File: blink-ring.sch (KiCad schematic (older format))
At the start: 35 parts, among them SW1 SW_SPDT, U1 ATtiny85_QFN20_1-5, U2 ATtiny85_QFN20_11-15

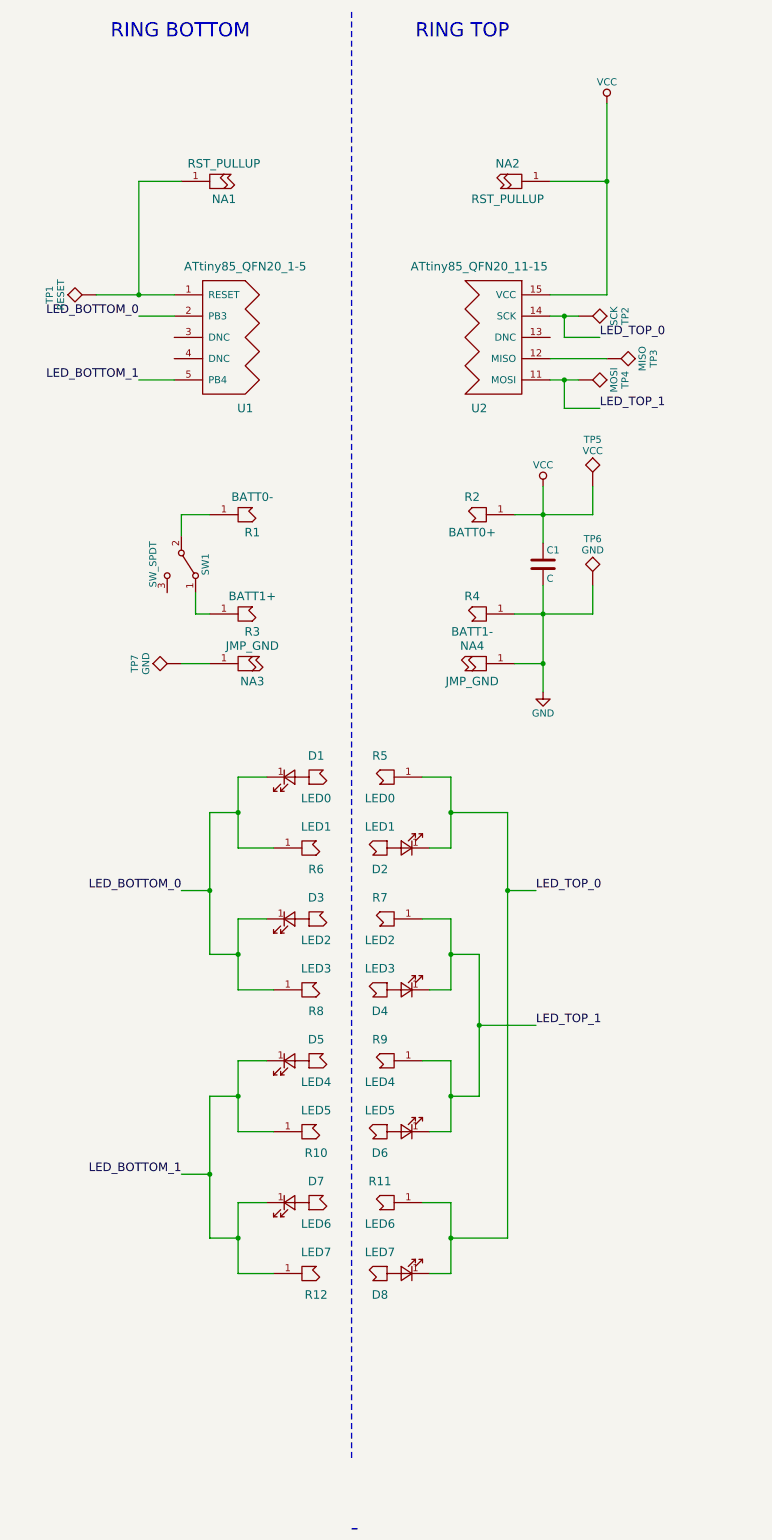
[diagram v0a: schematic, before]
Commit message: finalized PCB outline and layout. ordered first rev.
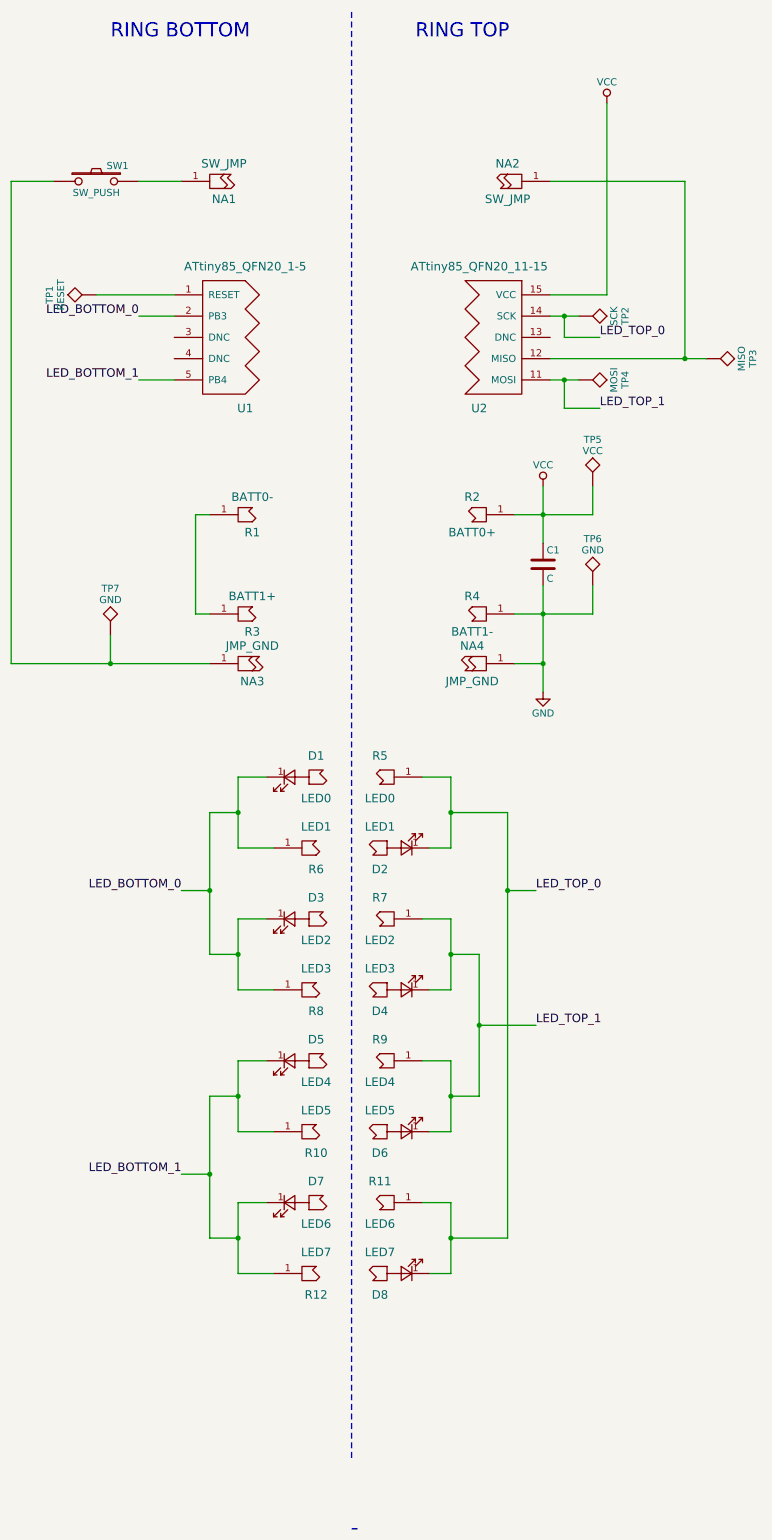
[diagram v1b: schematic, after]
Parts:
- removed SW1: SW_SPDT, KiCad_Footprints:ZF_SW_PCM12SMTR, symbol SW_SPDT
- added SW1: SW_PUSH, KiCad_Footprints:ZF_SW_B3U, symbol SW_PUSH
- NA1, NA2: value RST_PULLUP -> SW_JMP
- R1, R4: footprint KiCad_Footprints:ZF_STRUCT_2-2_HOLE -> KiCad_Footprints:ZF_BATT_AC10E_NEG
- R2, R3: footprint KiCad_Footprints:ZF_STRUCT_2-2_HOLE -> KiCad_Footprints:ZF_BATT_AC10E_POS
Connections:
- net VCC: no longer NA2.1
- net at TP1.1, U1.1 (RESET): no longer NA1.1
- net at TP3.1, U2.12 (MISO): now also NA2.1
- net at R1.1: now also R3.1
- net at NA3.1, TP7.1: now also SW1.1
- new net: NA1.1, SW1.2
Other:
- moved on the sheet: TP3, TP7
